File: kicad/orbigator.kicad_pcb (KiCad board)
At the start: 2 copper layers, 70 x 55 mm, 4 parts

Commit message: PCB layout WiP
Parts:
- added DISP1: OLED_Encoder, orbigator:PinSocket_1x09_P2.54mm_Vertical, F.Cu at (84.5, 138.4)
- added J1: Conn_01x01, orbigator:PinHeader_1x01_P2.54mm_Vertical, F.Cu at (145.3, 123.2)
- added J10: Conn_01x01, orbigator:PinHeader_1x01_P2.54mm_Vertical, F.Cu at (149.9, 132.4)
- added J11: Conn_01x01, orbigator:PinHeader_1x01_P2.54mm_Vertical, F.Cu at (149.9, 137.0)
- added J12: Conn_01x01, orbigator:PinHeader_1x01_P2.54mm_Vertical, F.Cu at (149.9, 141.6)
- added J13: Conn_01x01, orbigator:PinHeader_1x01_P2.54mm_Vertical, F.Cu at (149.9, 146.2)
- added J14: Conn_01x01, orbigator:PinHeader_1x01_P2.54mm_Vertical, F.Cu at (149.9, 150.8)
- added J15: Conn_01x01, orbigator:PinHeader_1x01_P2.54mm_Vertical, F.Cu at (154.4, 123.2)
- added J16: Conn_01x01, orbigator:PinHeader_1x01_P2.54mm_Vertical, F.Cu at (154.4, 127.8)
- added J17: Conn_01x01, orbigator:PinHeader_1x01_P2.54mm_Vertical, F.Cu at (154.4, 132.4)
- added J18: Conn_01x01, orbigator:PinHeader_1x01_P2.54mm_Vertical, F.Cu at (154.4, 137.0)
- added J19: Conn_01x01, orbigator:PinHeader_1x01_P2.54mm_Vertical, F.Cu at (154.4, 141.6)
- added J2: Conn_01x01, orbigator:PinHeader_1x01_P2.54mm_Vertical, F.Cu at (145.3, 127.8)
- added J20: Conn_01x01, orbigator:PinHeader_1x01_P2.54mm_Vertical, F.Cu at (154.4, 146.2)
- added J21: Conn_01x01, orbigator:PinHeader_1x01_P2.54mm_Vertical, F.Cu at (154.4, 150.8)
- added J22: Conn_01x01, orbigator:PinHeader_1x01_P2.54mm_Vertical, F.Cu at (159.0, 123.2)
- added J23: Conn_01x01, orbigator:PinHeader_1x01_P2.54mm_Vertical, F.Cu at (159.0, 127.8)
- added J24: Conn_01x01, orbigator:PinHeader_1x01_P2.54mm_Vertical, F.Cu at (159.0, 132.4)
- added J25: Conn_01x01, orbigator:PinHeader_1x01_P2.54mm_Vertical, F.Cu at (159.0, 137.0)
- added J26: Conn_01x01, orbigator:PinHeader_1x01_P2.54mm_Vertical, F.Cu at (159.0, 141.6)
- added J3: Conn_01x01, orbigator:PinHeader_1x01_P2.54mm_Vertical, F.Cu at (145.3, 132.4)
- added J4: Conn_01x01, orbigator:PinHeader_1x01_P2.54mm_Vertical, F.Cu at (145.3, 137.0)
- added J5: Conn_01x01, orbigator:PinHeader_1x01_P2.54mm_Vertical, F.Cu at (145.3, 141.6)
- added J6: Conn_01x01, orbigator:PinHeader_1x01_P2.54mm_Vertical, F.Cu at (145.3, 146.2)
- added J7: Conn_01x01, orbigator:PinHeader_1x01_P2.54mm_Vertical, F.Cu at (145.3, 150.8)
- added J8: Conn_01x01, orbigator:PinHeader_1x01_P2.54mm_Vertical, F.Cu at (149.9, 123.2)
- added J9: Conn_01x01, orbigator:PinHeader_1x01_P2.54mm_Vertical, F.Cu at (149.9, 127.8)
- added M1: DYNAMIXEL_1, orbigator:JST_GH_BM03B-GHS-TBT_1x03-1MP_P1.25mm_Vertical, F.Cu at (135.9, 143.5)
- added M2: DYNAMIXEL_2, orbigator:JST_GH_BM03B-GHS-TBT_1x03-1MP_P1.25mm_Vertical, F.Cu at (135.8, 152.3)
- added R1: 10k, orbigator:R_Axial_DIN0207_L6.3mm_D2.5mm_P7.62mm_Horizontal, F.Cu at (83.8, 125.7)
- added R2: 10k, orbigator:R_Axial_DIN0207_L6.3mm_D2.5mm_P7.62mm_Horizontal, F.Cu at (83.8, 132.1)
- added R3: 10k, orbigator:R_Axial_DIN0207_L6.3mm_D2.5mm_P7.62mm_Horizontal, F.Cu at (83.8, 128.9)
- added RTC1: DS3232, orbigator:DS3232_RTC, F.Cu at (91.3, 148.6)
- added U1: Pico_2, orbigator:RaspberryPi_Pico_SMD_HandSolder, F.Cu at (106.7, 147.3)
- added U2: 74LS126, orbigator:DIP-14_W7.62mm, F.Cu at (121.3, 140.3)
- H1, H2, H3, H4: footprint MountingHole:MountingHole_3.2mm_M3 -> orbigator:MountingHole_3.2mm_M3

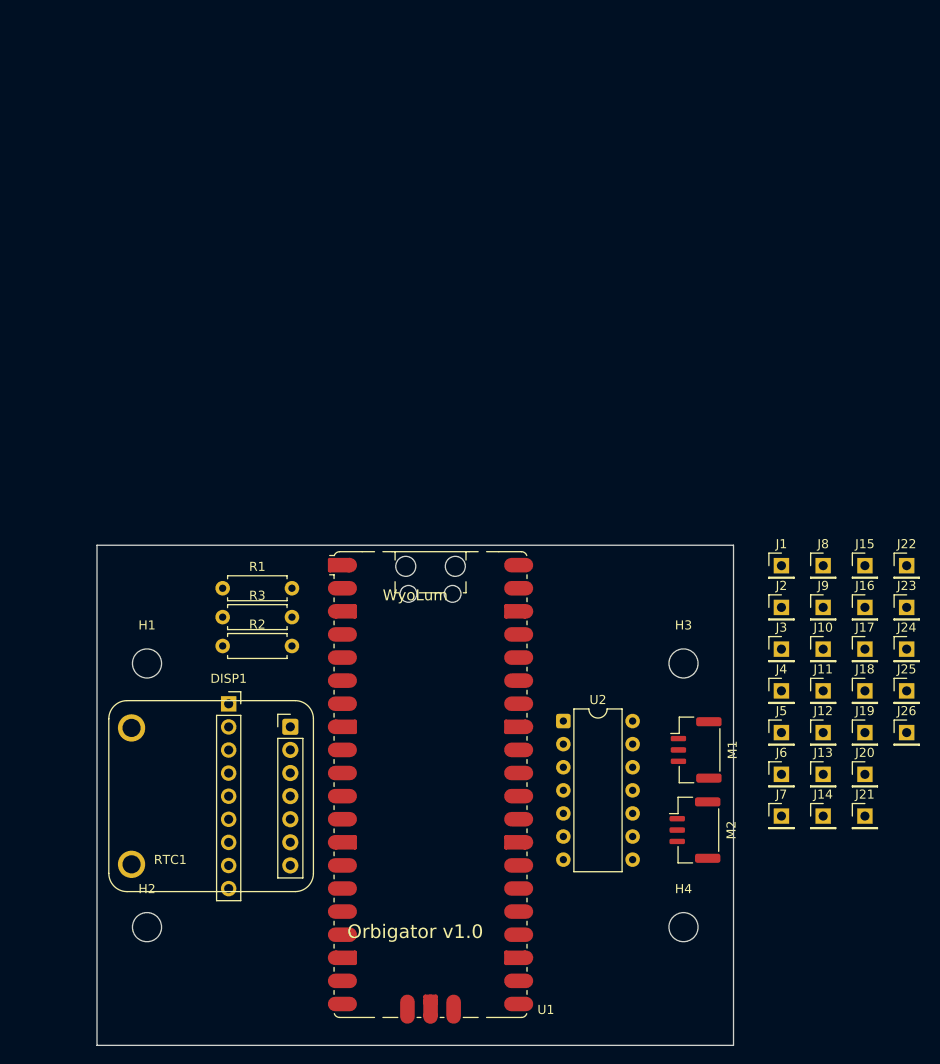
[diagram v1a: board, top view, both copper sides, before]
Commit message: PCB check parts placement
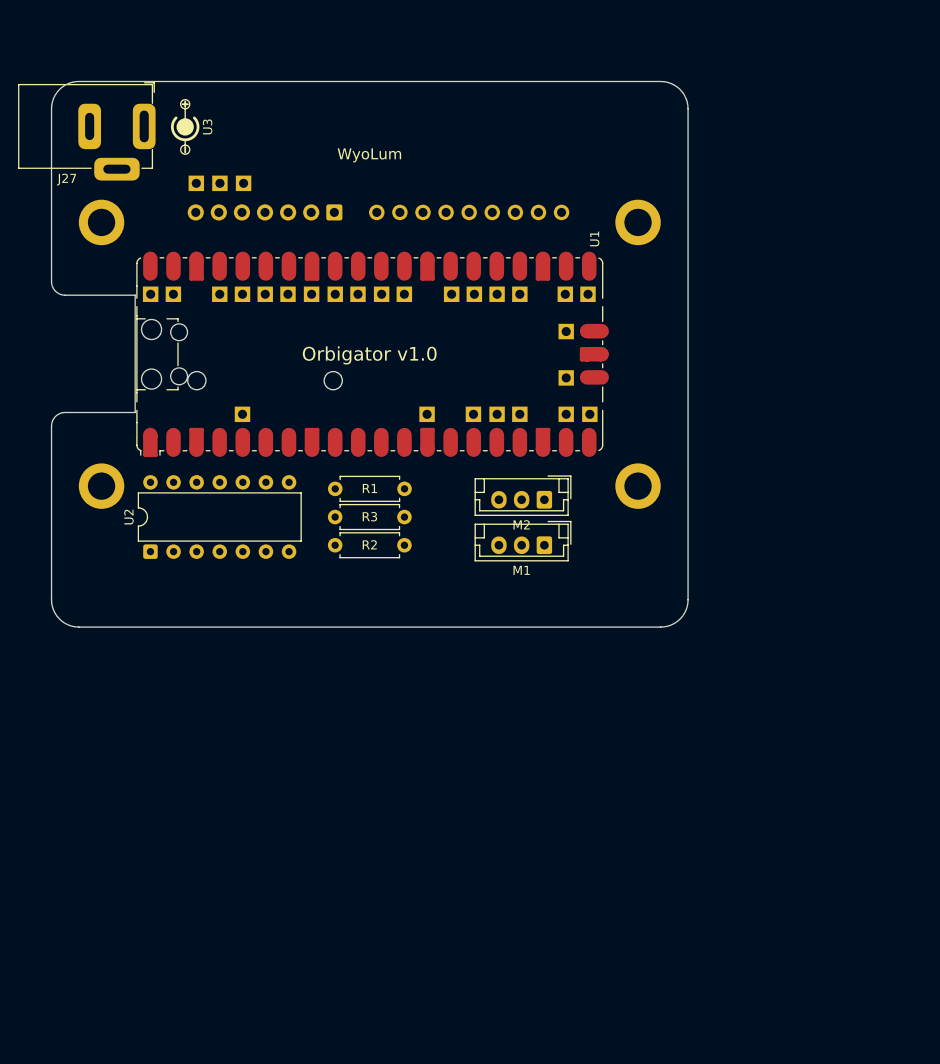
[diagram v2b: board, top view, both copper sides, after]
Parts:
- removed H1, H2, H3, H4: MountingHole, orbigator:MountingHole_3.2mm_M3
- added J27: Barrel_Jack_Switch, orbigator:BarrelJack_Horizontal, F.Cu at (75.2, 74.9)
- added J28: Conn_01x01, orbigator:PinHeader_1x01_P2.54mm_Vertical, F.Cu at (86.1, 81.2)
- added J29: Conn_01x01, orbigator:PinHeader_1x01_P2.54mm_Vertical, F.Cu at (83.5, 81.2)
- added J30: Conn_01x01, orbigator:PinHeader_1x01_P2.54mm_Vertical, F.Cu at (80.9, 81.2)
- added U3: DC_polarity, orbigator:DC, F.Cu at (79.7, 75.0)
- DISP1: footprint orbigator:PinSocket_1x09_P2.54mm_Vertical -> orbigator:OLED_ENC2; moved to B.Cu
- M1, M2: footprint orbigator:JST_GH_BM03B-GHS-TBT_1x03-1MP_P1.25mm_Vertical -> orbigator:JST_EH_B3B-EH-A_1x03_P2.50mm_Vertical
- RTC1: moved to B.Cu
- moved J25 93.9 mm to (75.9, 93.4)
- moved J24 89.6 mm to (78.4, 93.4)
- moved J13 84.8 mm to (83.5, 93.4)
- moved J23 80.8 mm to (86.0, 93.4)
- moved J20 79.1 mm to (86.0, 106.6)
- moved J14 75.2 mm to (101.3, 93.4)
- moved J12 74.1 mm to (93.6, 93.4)
- moved J11 73.3 mm to (91.0, 93.4)
- moved J7 70.8 mm to (103.8, 93.4)
- moved J8 68.2 mm to (88.5, 93.4)
- moved J10 66.4 mm to (96.2, 93.4)
- moved RTC1 64.3 mm to (88.5, 84.4), turned to 90 degrees
- moved J6 64.1 mm to (109.0, 93.4)
- moved J26 63.3 mm to (106.3, 106.6)
- moved J21 62.6 mm to (121.6, 97.5)
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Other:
- board size 70 x 55 mm -> 70 x 60 mm

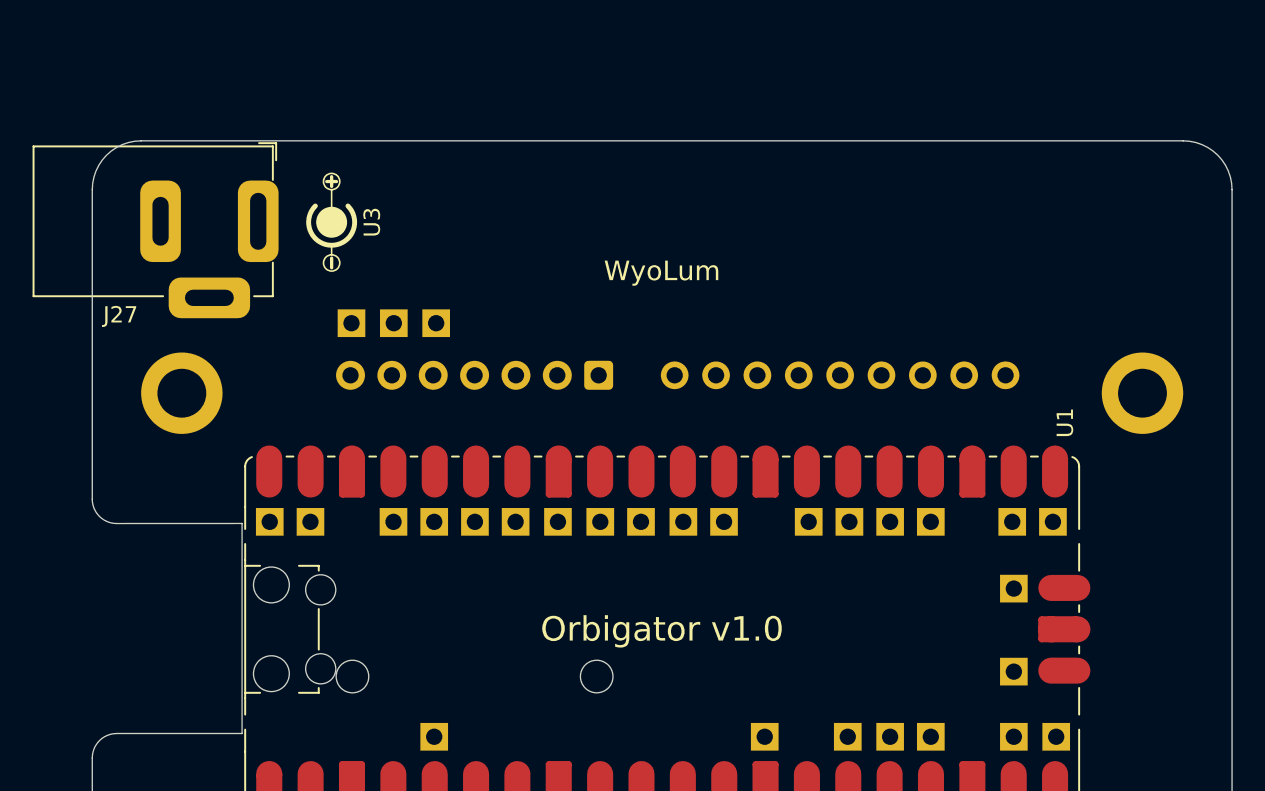
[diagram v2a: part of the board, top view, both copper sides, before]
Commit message: PCB modified RTC layout
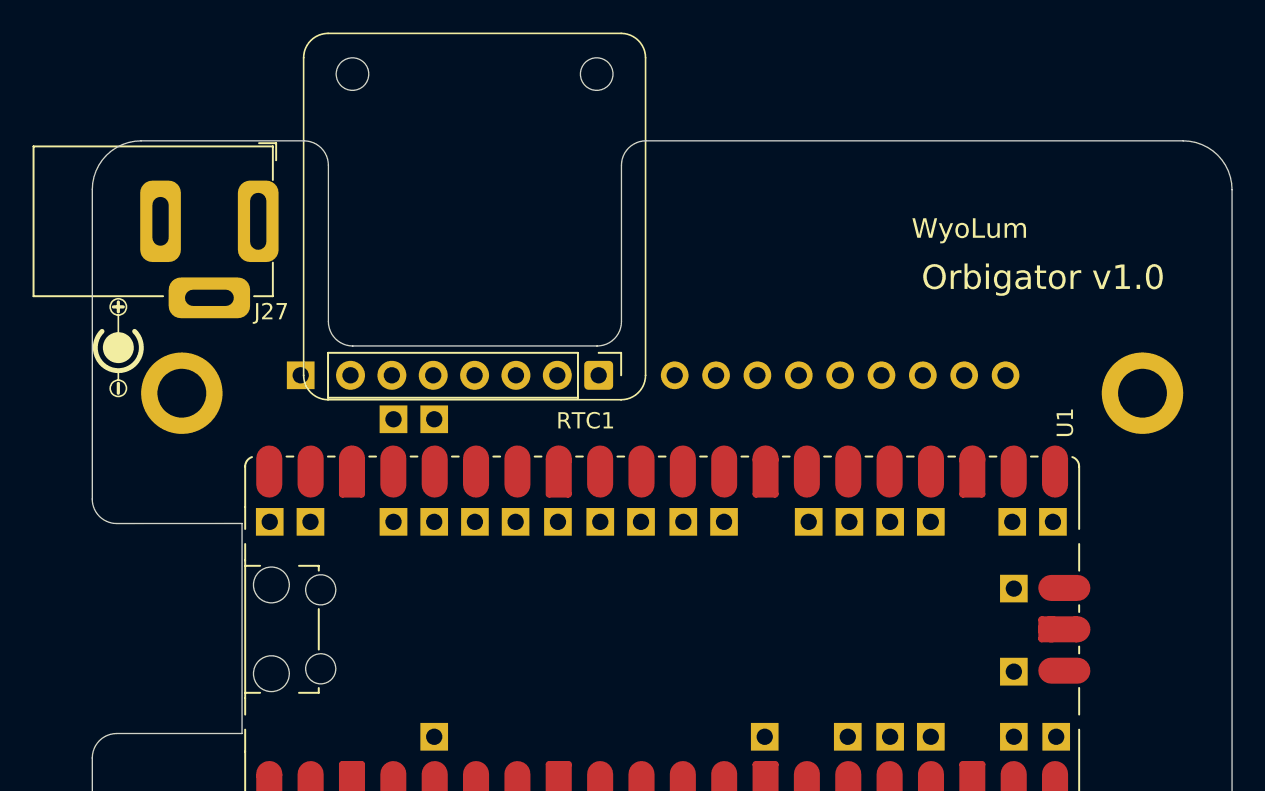
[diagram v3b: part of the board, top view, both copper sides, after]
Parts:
- RTC1: moved to F.Cu
- moved U3 15.2 mm to (66.6, 82.7)
- moved J28 5.90 mm to (86.0, 87.1)
- moved J29 5.90 mm to (83.5, 87.1)
- moved J30 4.47 mm to (77.8, 84.4)
- turned RTC1 to -90 degrees
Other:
- outline, holes or cut-outs redrawn

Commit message: PCB layout done
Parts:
- added G1: Logo-WL3, orbigator:logo-WL3, F.Cu at (124.6, 96.3)
- added J31: Conn_01x01, orbigator:PinHeader_1x01_P2.54mm_Vertical, F.Cu at (82.0, 115.3)
- added J32: Conn_01x01, orbigator:PinHeader_1x01_P2.54mm_Vertical, F.Cu at (129.5, 102.6)
- added J33: Conn_01x01, orbigator:PinHeader_1x01_P2.54mm_Vertical, F.Cu at (94.8, 115.4)
- added J34: Conn_01x01, orbigator:PinHeader_1x01_P2.54mm_Vertical, F.Cu at (82.0, 89.6)
- added J35: Conn_01x01, orbigator:PinHeader_1x01_P2.54mm_Vertical, F.Cu at (120.2, 115.4)
- added J36: Conn_01x01, orbigator:PinHeader_1x01_P2.54mm_Vertical, F.Cu at (120.1, 89.6)
- added J37: Conn_01x01, orbigator:PinHeader_1x01_P2.54mm_Vertical, F.Cu at (107.5, 89.6)
- RTC1: moved to B.Cu
- moved J27 70.6 mm to (124.8, 125.2), turned to 180 degrees
- moved U3 68.5 mm to (120.3, 125.2)
- moved J30 18.3 mm to (96.0, 86.1), turned to 180 degrees
- moved R1 12.6 mm to (102.6, 127.3)
- moved J29 10.0 mm to (93.5, 86.1), turned to 180 degrees
- moved J20 8.87 mm to (87.1, 115.4)
- moved J15 8.87 mm to (125.3, 115.4)
- moved J16 8.87 mm to (122.7, 115.4)
- moved J26 8.87 mm to (107.4, 115.4)
- moved J19 8.87 mm to (112.5, 115.4)
- moved J17 8.87 mm to (117.6, 115.4)
- moved J18 8.87 mm to (115.1, 115.4)
- moved M1 8.58 mm to (113.4, 127.3)
- moved R3 8.51 mm to (102.6, 123.5), turned to 180 degrees
- moved J21 8.29 mm to (129.5, 100.0)
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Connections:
- J12 pad 1: Net-(J12-Pin_1) -> /GND
- U1 pad 33: Net-(J12-Pin_1) -> /GND
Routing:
- net /GND: track 0.00 -> 289.2 mm
- net /3V3: track 0.00 -> 186.4 mm
- net /5V0: track 0.00 -> 84.9 mm
- net /SCL: track 0.00 -> 80.4 mm, vias 0 -> 1
- net /SDA: track 0.00 -> 78.8 mm, vias 0 -> 1
- net /MOT_DAT: track 0.00 -> 63.4 mm
- net /CNF_BTN: track 0.00 -> 45.8 mm, vias 0 -> 3
- net /ENC_SW: track 0.00 -> 42.8 mm
- net /ENC_B: track 0.00 -> 33.4 mm
- net /ENC_A: track 0.00 -> 33.4 mm
- net /BAK_BTN: track 0.00 -> 32.4 mm
- net /DIR: track 0.00 -> 31.1 mm
- net /UART_TX: track 0.00 -> 23.7 mm
- net Net-(J22-Pin_1): track 0.00 -> 4.47 mm
- net Net-(J21-Pin_1): track 0.00 -> 4.47 mm
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- added copper zone on B.Cu, net /GND
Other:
- board size 70 x 60 mm -> 70 x 47.5 mm
